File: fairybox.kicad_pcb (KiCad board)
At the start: 2 copper layers, 91.4 x 55.9 mm, 65 parts, among them J1 REED, Q1 locked, Q10 locked, Q2 locked, Q3 locked, Q4 locked, Q5 locked, Q6 locked, Q7 locked, Q8 locked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

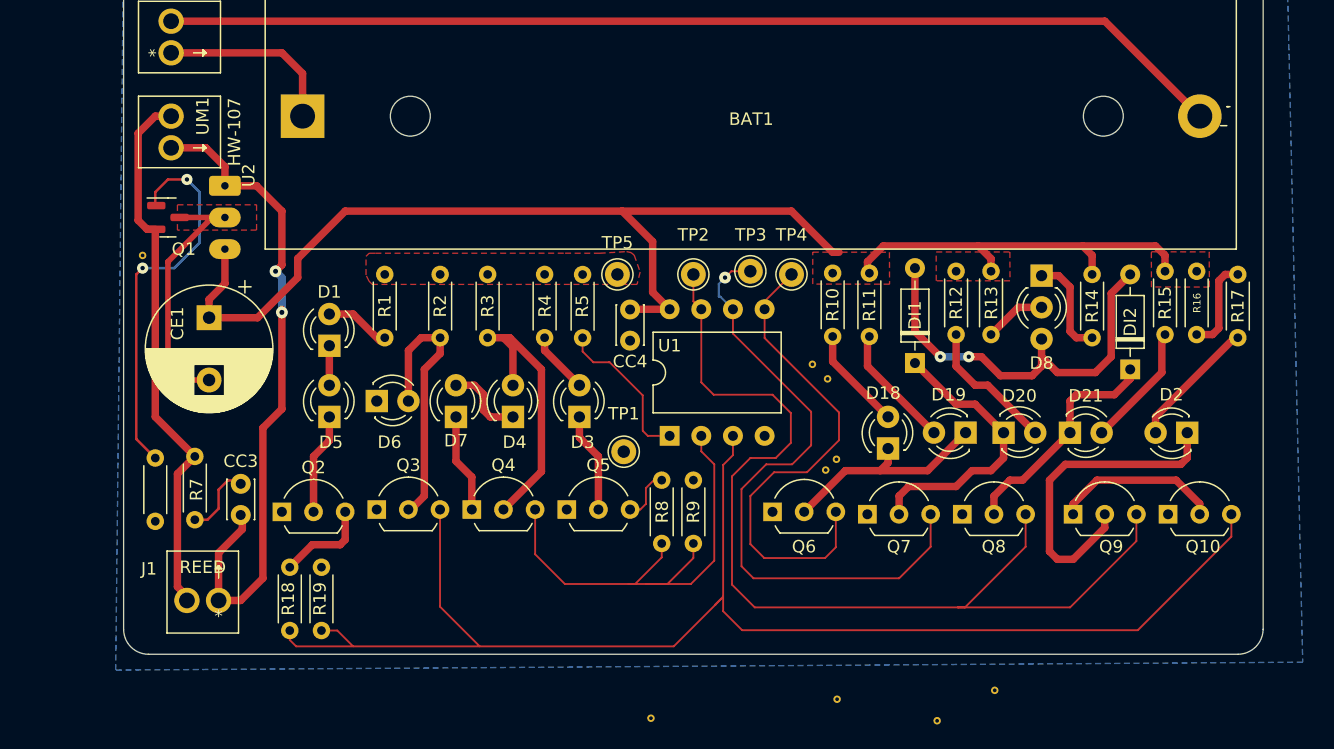
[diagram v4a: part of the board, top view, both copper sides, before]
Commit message: Updated solder mask labels
Moved component reference designators around. Added some informational text to the solder mask
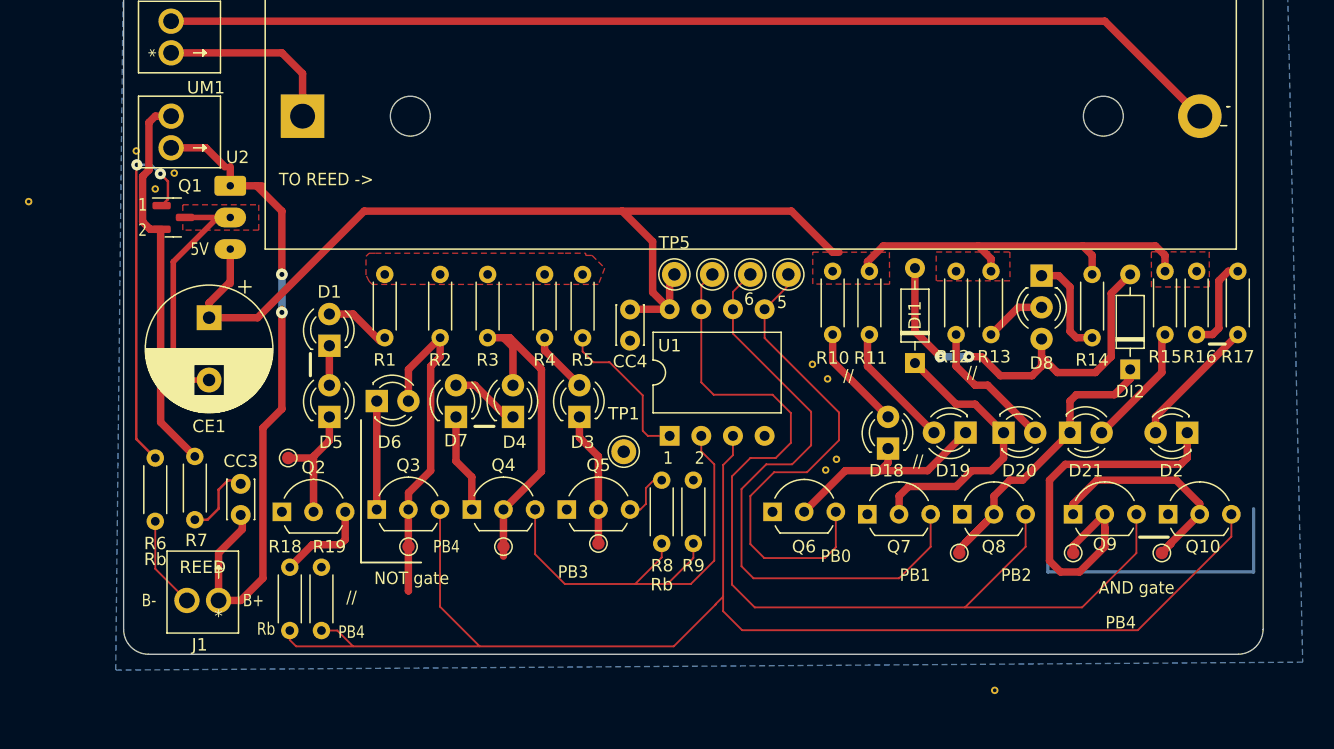
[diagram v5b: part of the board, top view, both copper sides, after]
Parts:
- added TP10: TestPoint_Small, TestPoint:TestPoint_Pad_D1.0mm, F.Cu at (117.9, 98.6)
- added TP11: TestPoint_Small, TestPoint:TestPoint_Pad_D1.0mm, F.Cu at (127.0, 98.6)
- added TP12: TestPoint_Small, TestPoint:TestPoint_Pad_D1.0mm, F.Cu at (134.1, 98.6)
- added TP6: TestPoint_Small, TestPoint:TestPoint_Pad_D1.0mm, F.Cu at (81.3, 98.0)
- added TP7: TestPoint_Small, TestPoint:TestPoint_Pad_D1.0mm, F.Cu at (73.7, 98.0)
- added TP8: TestPoint_Small, TestPoint:TestPoint_Pad_D1.0mm, F.Cu at (64.0, 90.9)
- added TP9: TestPoint_Small, TestPoint:TestPoint_Pad_D1.0mm, F.Cu at (88.9, 97.8)
- moved JP8 76.2 mm to (43.2, 70.4)
- moved JP5 75.4 mm to (54.9, 68.1)
- moved JP2 58.2 mm to (53.3, 69.3)
- moved JP1 8.40 mm to (51.8, 66.3)
- moved TP5 4.57 mm to (95.0, 76.2)
- moved TP2 1.52 mm to (98.0, 76.2)
- moved U2 0.43 mm to (59.4, 69.1)
- moved Q1 0.43 mm to (54.8, 71.6)
- moved R17 0.25 mm to (140.2, 75.9)
- moved TP3 0.25 mm to (101.1, 76.2)
- moved TP4 0.25 mm to (104.1, 76.2)
- moved R10 0.15 mm to (107.7, 75.9)
- moved R11 0.15 mm to (110.6, 75.9)
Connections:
- J1 pad 2: -BATT -> /REED_RETURN
- Q3 pad 1: unconnected-(Q3-Pad1) -> GND
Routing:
- net -BATT: track 43.7 -> 31.2 mm
- net GND: track 29.3 -> 38.0 mm
- net /Q8_COL: track 18.3 -> 25.8 mm
- net /REED_RETURN: track 0.00 -> 7.40 mm
- net /Q9_COL: track 26.4 -> 33.2 mm
- net /Q3_COL: track 22.0 -> 27.7 mm
- net /Q10_COL: track 13.4 -> 18.1 mm
- net /Q4_COL: track 22.0 -> 25.7 mm
- net /Q5_COL: track 8.07 -> 10.8 mm
- net +5V: track 106.8 -> 109.2 mm
- net /MCU GPIO3: track 40.7 -> 38.4 mm
- net /MCU GPIO1 MISO: track 51.5 -> 49.4 mm, vias 1 -> 0
- net /Q2_COL: track 8.15 -> 10.2 mm
- net /Q1_BASE: track 31.0 -> 29.4 mm
- net /D7_AN: track 6.37 -> 5.62 mm
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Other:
- board text added: "//"
- board text added: "1"
- board text added: "2"
- board text added: "5"
- board text added: "5V"
- board text added: "6"
- board text added: "AND gate"
- board text added: "B+"
- board text added: "B-"
- board text added: "NOT gate"
- board text added: "PB0"
- board text added: "PB1"
- board text added: "PB2"
- board text added: "PB3"
- board text added: "PB4"
- board text added: "Rb"
- board text added: "TO REED ->"

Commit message: Cleanup
alignment and other misc changes.
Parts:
- TP6, TP7: value TestPoint_Small -> TP
- TP9: value TestPoint_Small -> tp
- moved JP9 47.9 mm to (62.5, 76.2)
- moved JP3 41.8 mm to (64.5, 79.2)
- moved JP6 27.4 mm to (92.3, 114.9)
- moved JP4 27.1 mm to (119.0, 82.5)
- moved JP7 9.55 mm to (116.8, 84.5)
- moved D4 2.57 mm to (82.4, 90.2)
- moved D7 2.54 mm to (77.5, 90.2)
- moved D6 2.54 mm to (71.1, 88.9)
- moved D3 2.53 mm to (87.4, 90.2)
- moved D5 2.53 mm to (67.3, 90.2)
- moved R4 1.06 mm to (83.7, 75.7)
- moved R2 0.71 mm to (75.7, 75.7)
- moved TP1 0.63 mm to (91.4, 90.8)
- moved TP9 0.63 mm to (88.9, 98.4)
- moved CC3 0.62 mm to (59.7, 95.9)
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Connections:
- R17 pad 1: /R17_AN -> +5V
- R5 pad 1: Net-(R5-Pad1) -> /SPI RST
- TP1 pad 1: +5V -> /SPI RST
- U1 pad 1: Net-(R5-Pad1) -> /SPI RST
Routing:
- net GND: track 38.0 -> 17.7 mm, vias 0 -> 1
- net /SPI RST: track 0.00 -> 18.3 mm
- net +5V: track 109.2 -> 125.3 mm
- net Net-(R5-Pad1): track 12.6 -> 0.00 mm
- net /R17_AN: track 7.74 -> 0.00 mm
- net /Q4_COL: track 25.7 -> 30.6 mm
- net /D3_AN: track 4.97 -> 8.42 mm
- net /Q8_COL: track 25.8 -> 23.0 mm
- net /D5_AN: track 3.17 -> 5.71 mm
- net /D2_AN: track 10.2 -> 12.4 mm
- net /Q6_COL: track 17.6 -> 19.7 mm
- net /D21_AN: track 9.62 -> 11.6 mm
- net /Q5_COL: track 10.8 -> 8.89 mm
- net /RP8: track 6.01 -> 4.31 mm
- net /D20_AN: track 11.1 -> 12.4 mm
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- removed copper zone on F.Cu, net +5V
- removed copper zone on F.Cu, net GND
